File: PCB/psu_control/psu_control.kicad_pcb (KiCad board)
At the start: 4 copper layers, 90 x 70 mm, 81 parts, among them J1 Vin (10-28V), J10 Vout (10-28V), J2 Vout (10-28V), J3 Vout (10-28V), J4 UART (isolated), J5 Vout (10-28V), J6 RRC-PMM240, J7 Amplifier 1 I2C, J8 Amplifier 2 I2C, J9 Other I2C, M1 5V FAN, M2 5V FAN, Q1 DMG9926USD, Q2 IPB80P04P4L04ATMA2, Q3 DMG9926USD, Q4 DMN6140L-13, Q5 SI2319DS-T1-GE3, Q6 DMN6140L-13, SW1 ON/OFF, U1 ISO7521C, U2 INA226, U3 Teensy_LC, U4 LM810M3-4.63, U5 V7805-1000

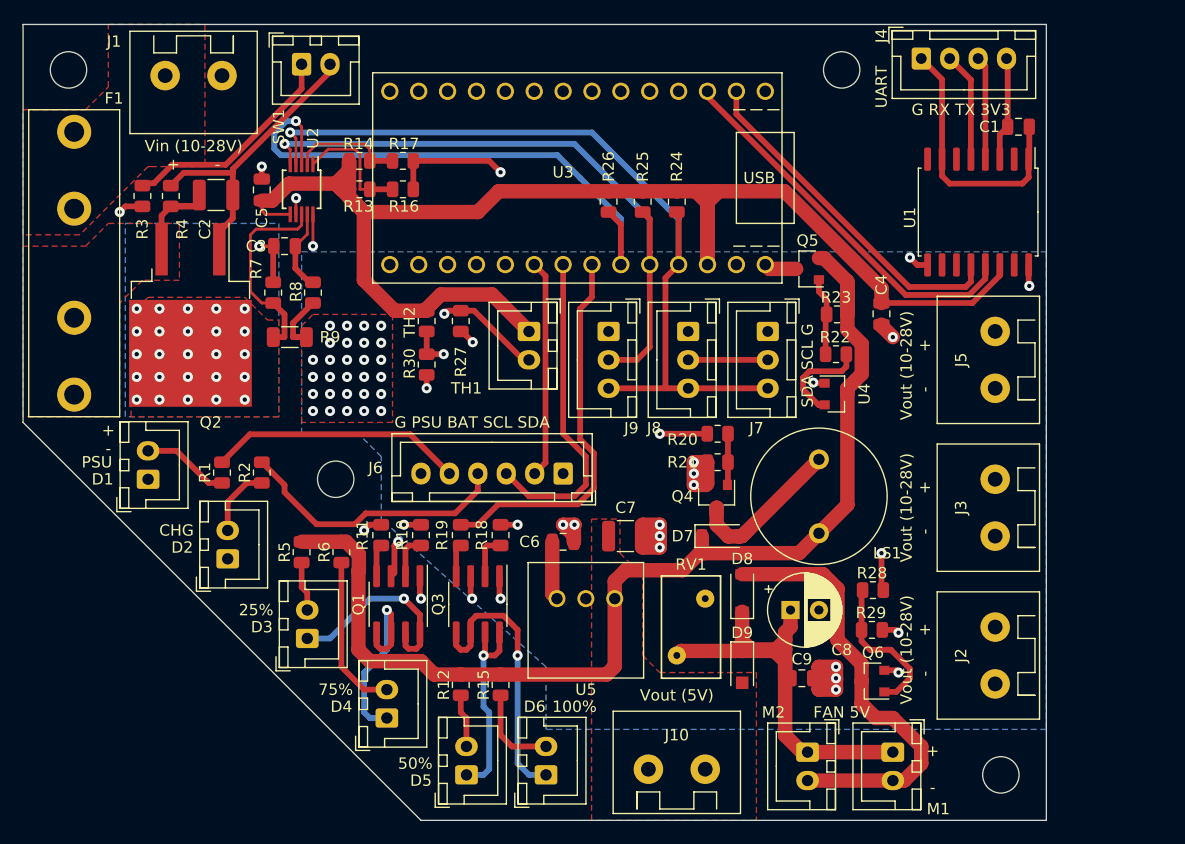
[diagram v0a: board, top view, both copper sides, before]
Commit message: Add first draft of psu_control
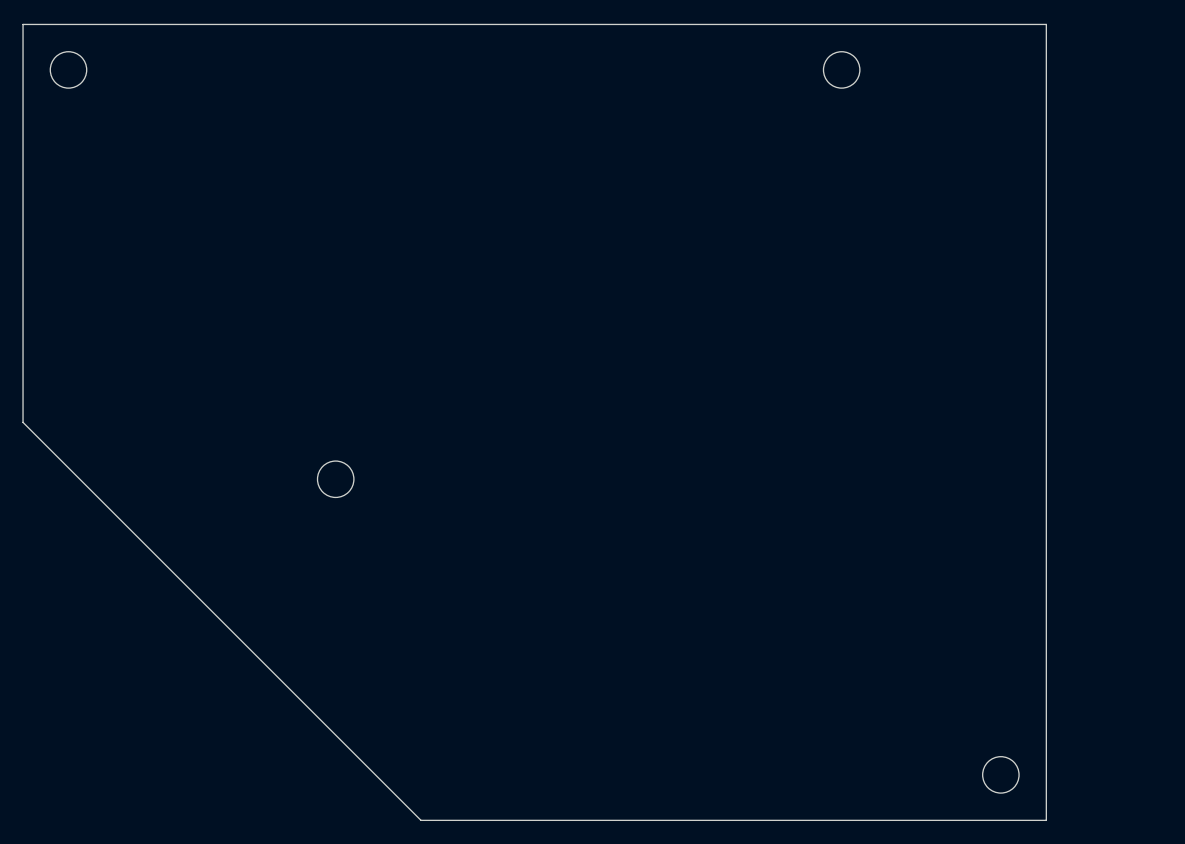
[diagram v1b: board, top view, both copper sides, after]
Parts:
- removed C1, C4, C5: 0.1µF/25V, Capacitor_SMD:C_0805_2012Metric
- removed C2, C7: 22µF/25V, Capacitor_SMD:C_1210_3225Metric
- removed C3: 1µF/10V, Capacitor_SMD:C_0805_2012Metric
- removed C6, C9: 10µF/50V, Capacitor_SMD:C_0805_2012Metric
- removed C8: 100µF/25V, Capacitor_THT:CP_Radial_D6.3mm_P2.50mm
- removed D1, D2: White, Connector_JST:JST_XH_B2B-XH-A_1x02_P2.50mm_Vertical
- removed D3: Red, Connector_JST:JST_XH_B2B-XH-A_1x02_P2.50mm_Vertical
- removed D4: Yellow, Connector_JST:JST_XH_B2B-XH-A_1x02_P2.50mm_Vertical
- removed D5: Amber, Connector_JST:JST_XH_B2B-XH-A_1x02_P2.50mm_Vertical
- removed D6: Green, Connector_JST:JST_XH_B2B-XH-A_1x02_P2.50mm_Vertical
- removed D7, D8: MBR160HWTR, Diode_SMD:D_SOD-123
- removed D9: DSS16UTR, Diode_SMD:D_SOD-123F
- removed F1: 10A Slow Blow, t-top:M205_FUSE
- removed J1: Vin (10-28V), t-top:OSTTA020161
- removed J10, J2, J3, J5: Vout (10-28V), t-top:OSTTA020161
- removed J4: UART (isolated), Connector_JST:JST_XH_B4B-XH-A_1x04_P2.50mm_Vertical
- removed J6: RRC-PMM240, Connector_JST:JST_XH_B6B-XH-A_1x06_P2.50mm_Vertical
- removed J7: Amplifier 1 I2C, Connector_JST:JST_XH_B3B-XH-A_1x03_P2.50mm_Vertical
- removed J8: Amplifier 2 I2C, Connector_JST:JST_XH_B3B-XH-A_1x03_P2.50mm_Vertical
- removed J9: Other I2C, Connector_JST:JST_XH_B3B-XH-A_1x03_P2.50mm_Vertical
- removed LS1: CEM-1206S, t-top:WT-1205
- removed M1, M2: 5V FAN, Connector_JST:JST_XH_B2B-XH-A_1x02_P2.50mm_Vertical
- removed Q1, Q3: DMG9926USD, Package_SO:SOIC-8_3.9x4.9mm_P1.27mm
- removed Q2: IPB80P04P4L04ATMA2, Package_TO_SOT_SMD:TO-263-2
- removed Q4, Q6: DMN6140L-13, Package_TO_SOT_SMD:SOT-23
- removed Q5: SI2319DS-T1-GE3, Package_TO_SOT_SMD:SOT-23
- removed R1, R2: 63.4, Resistor_SMD:R_0805_2012Metric
- removed R10, R11, R18, R19, R20, R28: 698, Resistor_SMD:R_0805_2012Metric
- removed R12, R15, R6: 365, Resistor_SMD:R_0805_2012Metric
- removed R13, R14, R16, R17: R, Resistor_SMD:R_0805_2012Metric
- removed R21, R23, R29, R3, R4: 100k, Resistor_SMD:R_0805_2012Metric
- removed R22: 511, Resistor_SMD:R_0805_2012Metric
- removed R24, R25: 1k, Resistor_SMD:R_0805_2012Metric
- removed R26, R27, R30: 10k, Resistor_SMD:R_0805_2012Metric
- removed R5: 374, Resistor_SMD:R_0805_2012Metric
- removed R7, R8: 10, Resistor_SMD:R_0805_2012Metric
- removed R9: 0.004, Resistor_SMD:R_1206_3216Metric
- removed RV1: V12ZA1P, Varistor:RV_Disc_D9mm_W5.2mm_P5mm
- removed SW1: ON/OFF, Connector_JST:JST_XH_B2B-XH-A_1x02_P2.50mm_Vertical
- removed TH1: 10K, Connector_JST:JST_XH_B2B-XH-A_1x02_P2.50mm_Vertical
- removed TH2: 10K, Resistor_SMD:R_0805_2012Metric
- removed U1: ISO7521C, Package_SO:SOIC-16W_7.5x10.3mm_P1.27mm
- removed U2: INA226, Package_SO:MSOP-10_3x3mm_P0.5mm
- removed U3: Teensy_LC, t-top:Teensy_LC
- removed U4: LM810M3-4.63, Package_TO_SOT_SMD:SOT-23
- removed U5: V7805-1000, t-top:V7805-1000
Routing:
- net +3V3: track 123.9 -> 0.00 mm
- net +5V: track 96.4 -> 0.00 mm
- net /SDA: track 74.4 -> 0.00 mm, vias 1 -> 0
- net /SCL: track 71.1 -> 0.00 mm, vias 1 -> 0
- net /BATTERY_STATUS: track 65.3 -> 0.00 mm
- net /CHARGER_STATUS: track 65.3 -> 0.00 mm
- net GND: track 64.1 -> 0.00 mm, vias 27 -> 0
- net /FAN_PWM: track 54.7 -> 0.00 mm, vias 1 -> 0
- net /BATTERY_50%: track 52.8 -> 0.00 mm, vias 1 -> 0
- net /ALERT: track 49.8 -> 0.00 mm, vias 1 -> 0
- net /BATTERY_75%: track 45.8 -> 0.00 mm, vias 1 -> 0
- net /BATTERY_25%: track 45.4 -> 0.00 mm, vias 1 -> 0
- net Net-(C8-Pad1): track 45.3 -> 0.00 mm
- net Net-(D8-Pad2): track 38.8 -> 0.00 mm
- net /UART_TX: track 33.9 -> 0.00 mm
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- removed copper zone on F.Cu, net +5V
- removed copper zone on B.Cu, net /VBUS
- removed copper zone on F.Cu, net /VBUS
- removed copper zone on B.Cu, net 10-28V
- removed copper zone on F.Cu, net 10-28V
- removed copper zone on In1.Cu, net GND
- removed copper zone on In2.Cu, net GND
- removed copper zone on F.Cu, net Net-(C2-Pad1)
- removed copper zone on F.Cu, net Net-(F1-Pad2)
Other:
- net class Default removed
- board text removed: "+ -"
- board text removed: "100%"
- board text removed: "25%"
- board text removed: "50%"
- board text removed: "75%"
- board text removed: "CHG"
- board text removed: "FAN 5V"
- board text removed: "G PSU BAT SCL SDA"
- board text removed: "G RX TX 3V3"
- board text removed: "PSU"
- board text removed: "SDA SCL G"
- board text removed: "UART"
- board text removed: "Vin (10-28V) + -"
- board text removed: "Vout (10-28V) - +"
- board text removed: "Vout (5V)"

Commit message: psu_control v4 is completed
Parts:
- removed the REF** at (19.0, 19.0)
- removed the REF** at (42.5, 55.0)
- removed the REF** at (87.0, 19.0)
- removed the REF** at (101.0, 81.0)
- added C1: 0.1µF/25V, Capacitor_SMD:C_0805_2012Metric, F.Cu at (37.0, 38.5)
- added C10: 10µF/25V, Capacitor_SMD:C_0805_2012Metric, F.Cu at (79.5, 32.0)
- added C11: 0.1µF/25V, Capacitor_SMD:C_0805_2012Metric, F.Cu at (33.5, 57.0)
- added C12: 0.1µF/25V, Capacitor_SMD:C_0805_2012Metric, F.Cu at (38.0, 60.0)
- added C13: 0.1µF/25V, Capacitor_SMD:C_0805_2012Metric, F.Cu at (38.0, 62.5)
- added C14: 0.1µF/25V, Capacitor_SMD:C_0805_2012Metric, F.Cu at (55.0, 45.5)
- added C15: 0.1µF/25V, Capacitor_SMD:C_0805_2012Metric, F.Cu at (43.5, 68.0)
- added C16: 0.1µF/25V, Capacitor_SMD:C_0805_2012Metric, F.Cu at (49.0, 74.0)
- added C17: 0.1µF/25V, Capacitor_SMD:C_0805_2012Metric, F.Cu at (113.5, 54.5)
- added C18: 0.1µF/25V, Capacitor_SMD:C_0805_2012Metric, F.Cu at (111.0, 47.0)
- added C19: 0.1µF/25V, Capacitor_SMD:C_0805_2012Metric, F.Cu at (108.5, 47.0)
- added C2: 2.2µF/25V, Capacitor_SMD:C_0805_2012Metric, F.Cu at (28.7, 43.0)
- added C20: 0.1µF/25V, Capacitor_SMD:C_0805_2012Metric, F.Cu at (113.5, 47.0)
- added C21: 0.1µF/25V, Capacitor_SMD:C_0805_2012Metric, F.Cu at (106.0, 47.0)
- added C3: 1µF/10V, Capacitor_SMD:C_0805_2012Metric, F.Cu at (34.5, 35.0)
- added C4: 22μF/10V, Capacitor_SMD:C_0805_2012Metric, F.Cu at (104.0, 27.9)
- added C5: 100µF/35V, Capacitor_THT:CP_Radial_D6.3mm_P2.50mm, F.Cu at (65.0, 21.3)
- added C6: 680µF/35V, Capacitor_THT:CP_Radial_D10.0mm_P5.00mm, F.Cu at (58.5, 30.1)
- added C7: 0.1µF/25V, Capacitor_SMD:C_0805_2012Metric, F.Cu at (40.0, 53.0)
- added C8: 0.1µF/25V, Capacitor_SMD:C_0805_2012Metric, F.Cu at (102.0, 35.0)
- added C9: 100µF/35V, Capacitor_THT:CP_Radial_D6.3mm_P2.50mm, F.Cu at (81.2, 37.0)
- added D1: DSS16U, Diode_SMD:D_SOD-123F, F.Cu at (78.4, 28.5)
- added D2: DSS16U, Diode_SMD:D_SOD-123F, F.Cu at (63.5, 38.5)
- added D3: DSS16U, Diode_SMD:D_SOD-123F, F.Cu at (104.9, 32.5)
- added D4: White, Connector_JST:JST_PH_B2B-PH-K_1x02_P2.00mm_Vertical, F.Cu at (102.0, 81.5)
- added D5: White, Connector_JST:JST_PH_B2B-PH-K_1x02_P2.00mm_Vertical, F.Cu at (94.5, 81.5)
- added F1: 10A Slow Blow, t-top:M205_FUSE, F.Cu at (19.1, 36.0)
- added J1: Vin (10-25V), t-top:OSTTA020161, F.Cu at (29.0, 19.0)
- added J10: Other 1 I2C, Connector_JST:JST_PH_B3B-PH-K_1x03_P2.00mm_Vertical, F.Cu at (112.5, 70.0)
- added J11: Light Sensor Front, Connector_JST:JST_PH_B3B-PH-K_1x03_P2.00mm_Vertical, F.Cu at (56.5, 81.5)
- added J12: Light Sensor Left, Connector_JST:JST_PH_B3B-PH-K_1x03_P2.00mm_Vertical, F.Cu at (66.0, 81.5)
- added J13: Light Sensor Back, Connector_JST:JST_PH_B3B-PH-K_1x03_P2.00mm_Vertical, F.Cu at (75.5, 81.5)
- added J14: Light Sensor Right, Connector_JST:JST_PH_B3B-PH-K_1x03_P2.00mm_Vertical, F.Cu at (85.0, 81.5)
- added J15: RRC-PMM240, Connector_JST:JST_PH_B5B-PH-K_1x05_P2.00mm_Vertical, F.Cu at (73.5, 71.0)
- added J16: RS232, Connector_JST:JST_PH_B3B-PH-K_1x03_P2.00mm_Vertical, F.Cu at (112.5, 60.0)
- added J2: Vout (10-25V), t-top:OSTTA020161, F.Cu at (41.5, 19.0)
- added J3: Vout (5V), Connector_JST:JST_XH_B2B-XH-A_1x02_P2.50mm_Vertical, F.Cu at (111.5, 25.8)
- added J4: Vout (10-25V), t-top:OSTTA020161, F.Cu at (54.0, 19.0)
- added J6: LED Strip, Connector_JST:JST_XH_B3B-XH-A_1x03_P2.50mm_Vertical, F.Cu at (111.5, 34.5)
- added J7: Amplifier 2 I2C, Connector_JST:JST_PH_B3B-PH-K_1x03_P2.00mm_Vertical, F.Cu at (94.5, 70.0)
- added J8: Amplifier 1 I2C, Connector_JST:JST_PH_B3B-PH-K_1x03_P2.00mm_Vertical, F.Cu at (100.5, 70.0)
- added J9: Amplifier 2 I2C, Connector_JST:JST_PH_B3B-PH-K_1x03_P2.00mm_Vertical, F.Cu at (106.5, 70.0)
- added L1: 22µH (NS12575T220MN), t-top:NS12575T220MN, F.Cu at (45.5, 34.5)
- added LS1: CEM-1206S, t-top:WT-1205, F.Cu at (70.5, 33.0)
- added M1: Fan, Connector_JST:JST_PH_B2B-PH-K_1x02_P2.00mm_Vertical, F.Cu at (90.0, 29.4)
- added M2: Fan, Connector_JST:JST_PH_B2B-PH-K_1x02_P2.00mm_Vertical, F.Cu at (97.5, 29.4)
- added Q1: SSM3J372R, Package_TO_SOT_SMD:SOT-23, F.Cu at (101.0, 59.0)
- added Q2: IPD042P03L3GATMA1, Package_TO_SOT_SMD:TO-252-2, F.Cu at (27.5, 33.3)
- added Q3: T2N7002AK, Package_TO_SOT_SMD:SOT-23, F.Cu at (26.5, 46.0)
- added Q4: AO4818B, Package_SO:SOIC-8_3.9x4.9mm_P1.27mm, F.Cu at (88.5, 37.5)
- added R1: 100k, Resistor_SMD:R_0805_2012Metric, F.Cu at (101.4, 49.5)
- added R10: 0, Resistor_SMD:R_0805_2012Metric, F.Cu at (37.1, 45.5)
- added R11: 10, Resistor_SMD:R_0805_2012Metric, F.Cu at (33.4, 31.9)
- added R12: 10, Resistor_SMD:R_0805_2012Metric, F.Cu at (35.9, 31.9)
- added R13: 100k, Resistor_SMD:R_0805_2012Metric, F.Cu at (30.4, 46.0)
- added R14: 0.004, Resistor_SMD:R_1206_3216Metric, F.Cu at (34.5, 27.0)
- added R15: 10k, Resistor_SMD:R_0805_2012Metric, F.Cu at (36.9, 51.0)
- added R16: NI, Resistor_SMD:R_0805_2012Metric, F.Cu at (67.3, 17.5)
- added R17: NI, Resistor_SMD:R_0805_2012Metric, F.Cu at (106.0, 20.0)
- added R18: 10k, Resistor_SMD:R_0805_2012Metric, F.Cu at (36.9, 54.0)
- added R19: NI, Resistor_SMD:R_0805_2012Metric, F.Cu at (62.9, 17.5)
- added R2: 511, Resistor_SMD:R_0805_2012Metric, F.Cu at (101.4, 52.5)
- added R20: NI, Resistor_SMD:R_0805_2012Metric, F.Cu at (106.0, 17.5)
- added R21: 698, Resistor_SMD:R_0805_2012Metric, F.Cu at (95.0, 38.8)
- added R22: 698, Resistor_SMD:R_0805_2012Metric, F.Cu at (98.5, 38.8)
- added R23: 100k, Resistor_SMD:R_0805_2012Metric, F.Cu at (95.0, 35.0)
- added R24: 100k, Resistor_SMD:R_0805_2012Metric, F.Cu at (98.5, 35.0)
- added R25: 10k, Resistor_SMD:R_0805_2012Metric, F.Cu at (64.5, 66.5)
- added R26: 10k, Resistor_SMD:R_0805_2012Metric, F.Cu at (61.0, 66.5)
- added R27: 10k, Resistor_SMD:R_0805_2012Metric, F.Cu at (25.5, 55.5)
- added R28: 10k, Resistor_SMD:R_0805_2012Metric, F.Cu at (31.0, 60.1)
- added R29: 10k, Resistor_SMD:R_0805_2012Metric, F.Cu at (36.5, 65.6)
- added R3: 2.2k, Resistor_SMD:R_0805_2012Metric, F.Cu at (94.0, 64.1)
- added R30: 10k, Resistor_SMD:R_0805_2012Metric, F.Cu at (29.3, 55.5)
- added R31: 10k, Resistor_SMD:R_0805_2012Metric, F.Cu at (34.0, 60.1)
- added R32: 10k, Resistor_SMD:R_0805_2012Metric, F.Cu at (39.5, 65.6)
- added R33: 10k, Resistor_SMD:R_0805_2012Metric, F.Cu at (42.0, 71.1)
- added R34: 10k, Resistor_SMD:R_0805_2012Metric, F.Cu at (47.5, 77.1)
- added R35: 10k, Resistor_SMD:R_0805_2012Metric, F.Cu at (45.0, 71.1)
- added R36: 10k, Resistor_SMD:R_0805_2012Metric, F.Cu at (50.5, 77.1)
- added R37: 63.4, Resistor_SMD:R_0805_2012Metric, F.Cu at (85.9, 70.0)
- added R38: 63.4, Resistor_SMD:R_0805_2012Metric, F.Cu at (85.9, 73.0)
- added R39: 698, Resistor_SMD:R_0805_2012Metric, F.Cu at (33.4, 46.8)
- added R4: 2.2k, Resistor_SMD:R_0805_2012Metric, F.Cu at (89.5, 64.0)
- added R40: 2.2k, Resistor_SMD:R_0805_2012Metric, F.Cu at (45.6, 48.5)
- added R41: 2.2k, Resistor_SMD:R_0805_2012Metric, F.Cu at (45.6, 45.5)
- added R5: 100k, Resistor_SMD:R_0805_2012Metric, F.Cu at (28.8, 40.5)
- added R6: 100k, Resistor_SMD:R_0805_2012Metric, F.Cu at (25.5, 42.1)
- added R7: 0, Resistor_SMD:R_0805_2012Metric, F.Cu at (40.9, 48.5)
- added R8: 0, Resistor_SMD:R_0805_2012Metric, F.Cu at (40.9, 45.5)
- added R9: 0, Resistor_SMD:R_0805_2012Metric, F.Cu at (37.1, 48.5)
- added REF**: MountingHole_3.2mm_M3, MountingHole:MountingHole_3.2mm_M3, F.Cu at (111.5, 81.5)
- added REF**: MountingHole_3.2mm_M3, MountingHole:MountingHole_3.2mm_M3, F.Cu at (111.5, 18.5)
- added REF**: MountingHole_3.2mm_M3, MountingHole:MountingHole_3.2mm_M3, F.Cu at (18.5, 18.5)
- added REF**: MountingHole_3.2mm_M3, MountingHole:MountingHole_3.2mm_M3, F.Cu at (18.5, 53.5)
- added RV1: V12ZA1P, Varistor:RV_Disc_D7mm_W4mm_P5mm, F.Cu at (83.6, 33.0)
- added SW1: Non-Momentary DPST, Connector_JST:JST_PH_B4B-PH-K_1x04_P2.00mm_Vertical, F.Cu at (26.0, 51.0)
- added SW2: SW_SPST, Connector_JST:JST_PH_B2B-PH-K_1x02_P2.00mm_Vertical, F.Cu at (25.0, 59.0)
- added SW3: SW_SPST, Connector_JST:JST_PH_B2B-PH-K_1x02_P2.00mm_Vertical, F.Cu at (30.5, 64.5)
- added SW4: SW_SPST, Connector_JST:JST_PH_B2B-PH-K_1x02_P2.00mm_Vertical, F.Cu at (36.0, 70.0)
- added SW5: SW_SPST, Connector_JST:JST_PH_B2B-PH-K_1x02_P2.00mm_Vertical, F.Cu at (41.5, 75.5)
- added SW6: SW_SPST, Connector_JST:JST_PH_B2B-PH-K_1x02_P2.00mm_Vertical, F.Cu at (49.0, 81.5)
- added TH1: 10k, Connector_JST:JST_PH_B2B-PH-K_1x02_P2.00mm_Vertical, F.Cu at (60.0, 71.0)
- added TH2: 10k, Resistor_SMD:R_0805_2012Metric, F.Cu at (57.5, 66.5)
- added U1: LM810M3-4.63, Package_TO_SOT_SMD:SOT-23, F.Cu at (101.0, 43.5)
- added U2: Teensy_LC, t-top:Teensy_LC, F.Cu at (79.3, 51.5)
- added U3: INA220, Package_SO:VSSOP-10_3x3mm_P0.5mm, F.Cu at (34.0, 39.8)
- added U4: K7805-3AR3, t-top:K7805-3AR3, F.Cu at (87.0, 18.0)
- added U5: 74HC14, Package_SO:TSSOP-14_4.4x5mm_P0.65mm, F.Cu at (57.0, 51.5)
- added U6: SN74LV1T34, Package_TO_SOT_SMD:SOT-23-5, F.Cu at (101.9, 38.5)
- added U7: MAX3221E, Package_SO:TSSOP-16_4.4x5mm_P0.65mm, F.Cu at (109.0, 53.0)
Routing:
- net /GENERAL_SDA: track 0.00 -> 107.6 mm, vias 0 -> 1
- net /GENERAL_SCL: track 0.00 -> 104.7 mm, vias 0 -> 2
- net /~{POWER_OFF}: track 0.00 -> 63.0 mm, vias 0 -> 1
- net GND: track 0.00 -> 60.5 mm, vias 0 -> 26
- net +5V: track 0.00 -> 54.9 mm, vias 0 -> 5
- net /LIGHT_SENSOR_RIGHT: track 0.00 -> 49.5 mm
- net Net-(C10-Pad1): track 0.00 -> 43.2 mm
- net /RS232/UART_TX: track 0.00 -> 41.9 mm
- net /LIGHT_SENSOR_BACK: track 0.00 -> 41.1 mm
- net +3.3V: track 0.00 -> 37.6 mm, vias 0 -> 14
- net /RS232/UART_RX: track 0.00 -> 36.7 mm
- net /POWER_SWITCH: track 0.00 -> 34.6 mm, vias 0 -> 1
- net Net-(C12-Pad1): track 0.00 -> 32.5 mm
- net /~{RS232_INVALID}: track 0.00 -> 32.0 mm
- net Net-(C11-Pad1): track 0.00 -> 31.7 mm
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- added copper zone on In2.Cu, net +3.3V
- added copper zone on F.Cu, net +5V
- added copper zone on In2.Cu, net +5V
- added copper zone on F.Cu, net 10-25V
- added copper zone on B.Cu, net GND
- added copper zone on F.Cu, net GND
- added copper zone on In1.Cu, net GND
- added copper zone on B.Cu, net Net-(C2-Pad1)
- added copper zone on F.Cu, net Net-(C2-Pad1)
- added copper zone on F.Cu, net Net-(C6-Pad1)
- added copper zone on F.Cu, net Net-(F1-Pad1)
- added copper zone on F.Cu, net Net-(R11-Pad2)
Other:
- board size 90 x 70 mm -> 100 x 70 mm
- board text added: "+ Vin - 10-25V"
- board text added: "+ Vout - 10-25V"
- board text added: "- +"
- board text added: "5V + Vout -"
- board text added: "Bat. S. - +"
- board text added: "Charg. S. - +"
- board text added: "G SCL SDA"
- board text added: "G SDA SCL BAT CHARG"
- board text added: "I2C"
- board text added: "LED 5V S G"
- board text added: "LS Back G S 3.3V"
- board text added: "LS Front G S 3.3V"
- board text added: "LS Left G S 3.3V"
- board text added: "LS Right G S 3.3V"
- board text added: "Other"
- board text added: "RRC-PMM240"
- board text added: "RS232 G RX TX"
- board text added: "START"
- board text added: "STOP"
- board text added: "V. D."
- board text added: "V. UP"

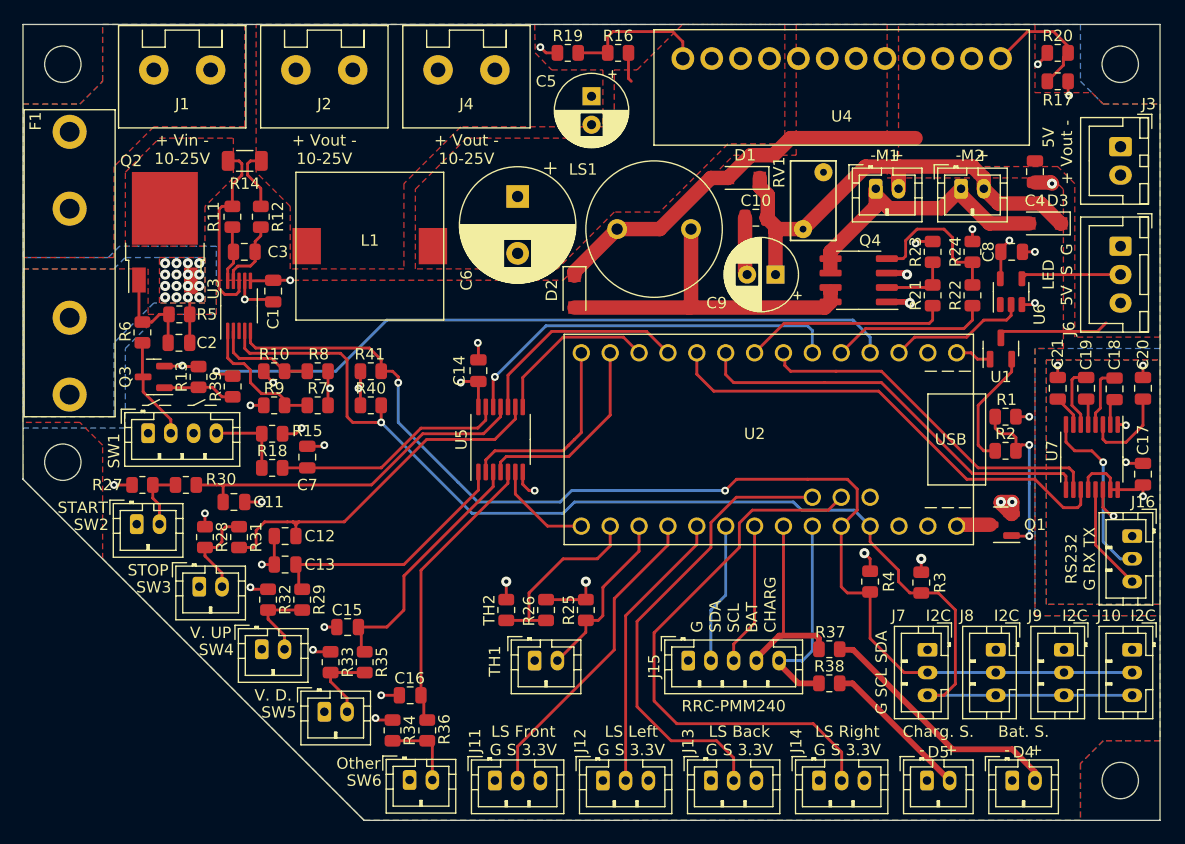
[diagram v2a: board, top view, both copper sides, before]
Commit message: Add dynamixel_control PCB
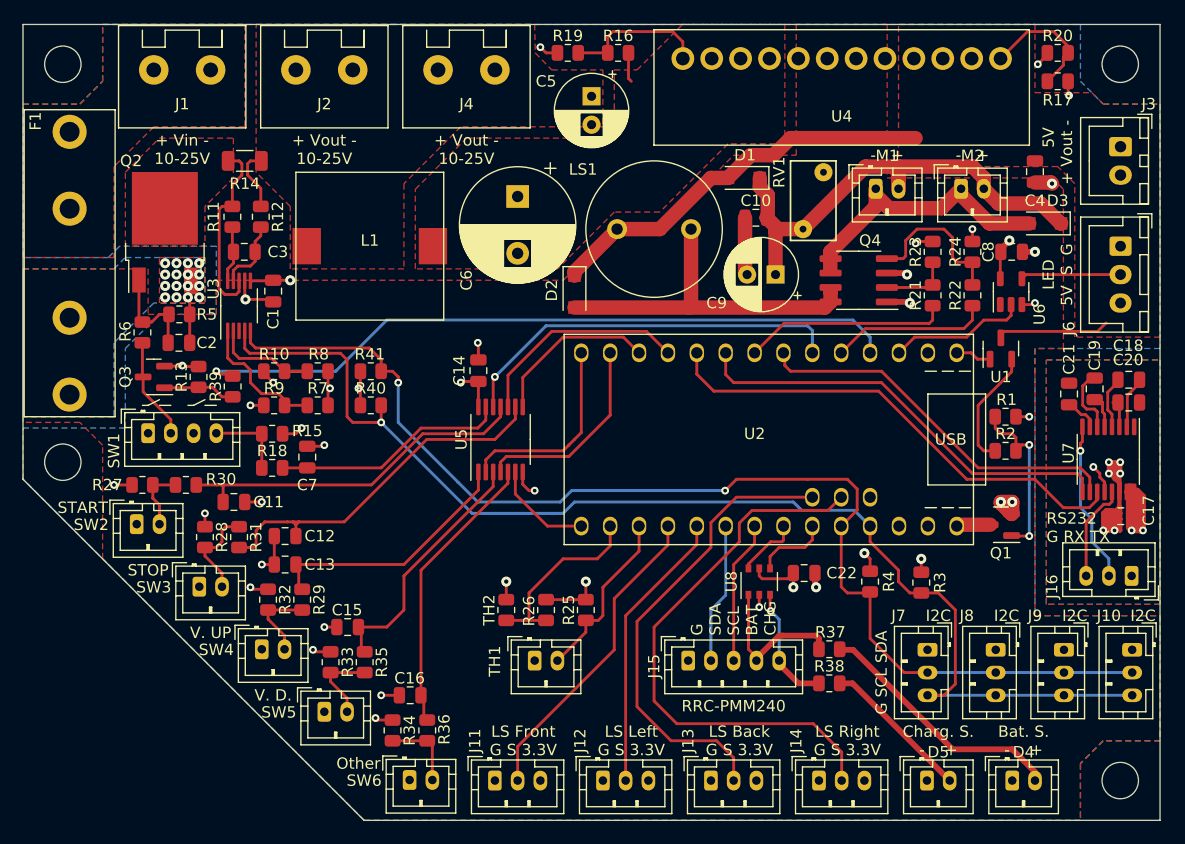
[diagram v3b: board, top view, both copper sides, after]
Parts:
- added C22: 0.1µF/25V, Capacitor_SMD:C_0805_2012Metric, F.Cu at (83.7, 63.2)
- added U8: 74LVC2G34, Package_SO:TSOP-6_1.65x3.05mm_P0.95mm, F.Cu at (79.8, 64.0)
- Q2: value IPD042P03L3GATMA1 -> IPD068P03L3GATMA1
- SW2, SW3, SW4, SW5, SW6: value SW_SPST -> BUTTON
- moved C17 4.18 mm to (111.5, 58.2), turned to 180 degrees
- moved J16 3.50 mm to (112.5, 63.5), turned to 180 degrees
- moved C20 1.77 mm to (112.2, 48.2), turned to 0 degrees
- moved C18 1.48 mm to (112.2, 46.2), turned to 180 degrees
- moved U7 1.46 mm to (110.5, 53.2)
- moved C21 1.12 mm to (107.0, 47.5)
- moved C19 0.75 mm to (109.2, 47.0)
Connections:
- J15 pad 4: /Battery/BATTERY_STATUS -> Net-(J15-Pad4)
- J15 pad 5: /Battery/CHARGER_STATUS -> Net-(J15-Pad5)
- Q2 pad 2: unconnected-(Q2-Pad2) -> Net-(Q2-Pad2)
- R11 pad 2: Net-(R11-Pad2) -> Net-(Q2-Pad2)
- R14 pad 1: Net-(R11-Pad2) -> Net-(Q2-Pad2)
- R37 pad 1: /Battery/BATTERY_STATUS -> Net-(J15-Pad4)
- R38 pad 1: /Battery/CHARGER_STATUS -> Net-(J15-Pad5)
- U3 pad 8: Net-(R11-Pad2) -> Net-(Q2-Pad2)
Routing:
- net GND: track 60.5 -> 91.5 mm, vias 26 -> 29
- net +3.3V: track 37.6 -> 57.0 mm, vias 14 -> 17
- net Net-(J15-Pad4): track 0.00 -> 18.9 mm
- net Net-(R11-Pad2): track 16.7 -> 0.00 mm
- net Net-(Q2-Pad2): track 0.00 -> 16.7 mm
- net /Battery/CHARGER_STATUS: track 18.8 -> 6.58 mm
- net /Battery/BATTERY_STATUS: track 17.3 -> 5.58 mm
- net Net-(J15-Pad5): track 0.00 -> 10.6 mm, vias 0 -> 1
- net Net-(C20-Pad1): track 7.85 -> 2.75 mm
- net Net-(C18-Pad1): track 2.34 -> 4.60 mm
- net /RS232/UART_RX: track 36.7 -> 38.3 mm
- net Net-(J16-Pad2): track 15.7 -> 14.2 mm
- net /~{RS232_INVALID}: track 32.0 -> 33.4 mm
- net /RS232/UART_TX: track 41.9 -> 42.9 mm
- net Net-(J16-Pad3): track 9.42 -> 8.62 mm
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- added copper zone on F.Cu, net Net-(Q2-Pad2)
- removed copper zone on F.Cu, net Net-(R11-Pad2)
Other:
- board text added: "G SDA SCL BAT CHG"
- board text removed: "G SDA SCL BAT CHARG"
